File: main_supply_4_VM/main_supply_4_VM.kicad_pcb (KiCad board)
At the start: 2 copper layers, 108.6 x 131.8 mm, 197 parts, among them J1 Conn_01x02_Pin, J2 A3_EN, J3 A3, J4 A2, J5 A2_EN, J6 FIL_EN, J7 FIL CAT FOCUS, J8 Conn_01x02_Pin, Q1 CSD19537Q3, Q2 Si7450DP, Q3 CSD19537Q3, Q4 STN0214, Q5 2N7002, T2 750315839, T3 YA9033-ALD, U1 LM5155DSSR, U10 TLV314QDBVR, U11 TLV314QDBVR, U12 Opamp_sep_pwr, U2 TLV314QDBVR, U3 LM5155DSSR, U4 PC817, U5 LM5155DSSR, U6 TL431DBZ, U7 AP2204K-5.0, U8 AP2204K-5.0, U9 AMC1311

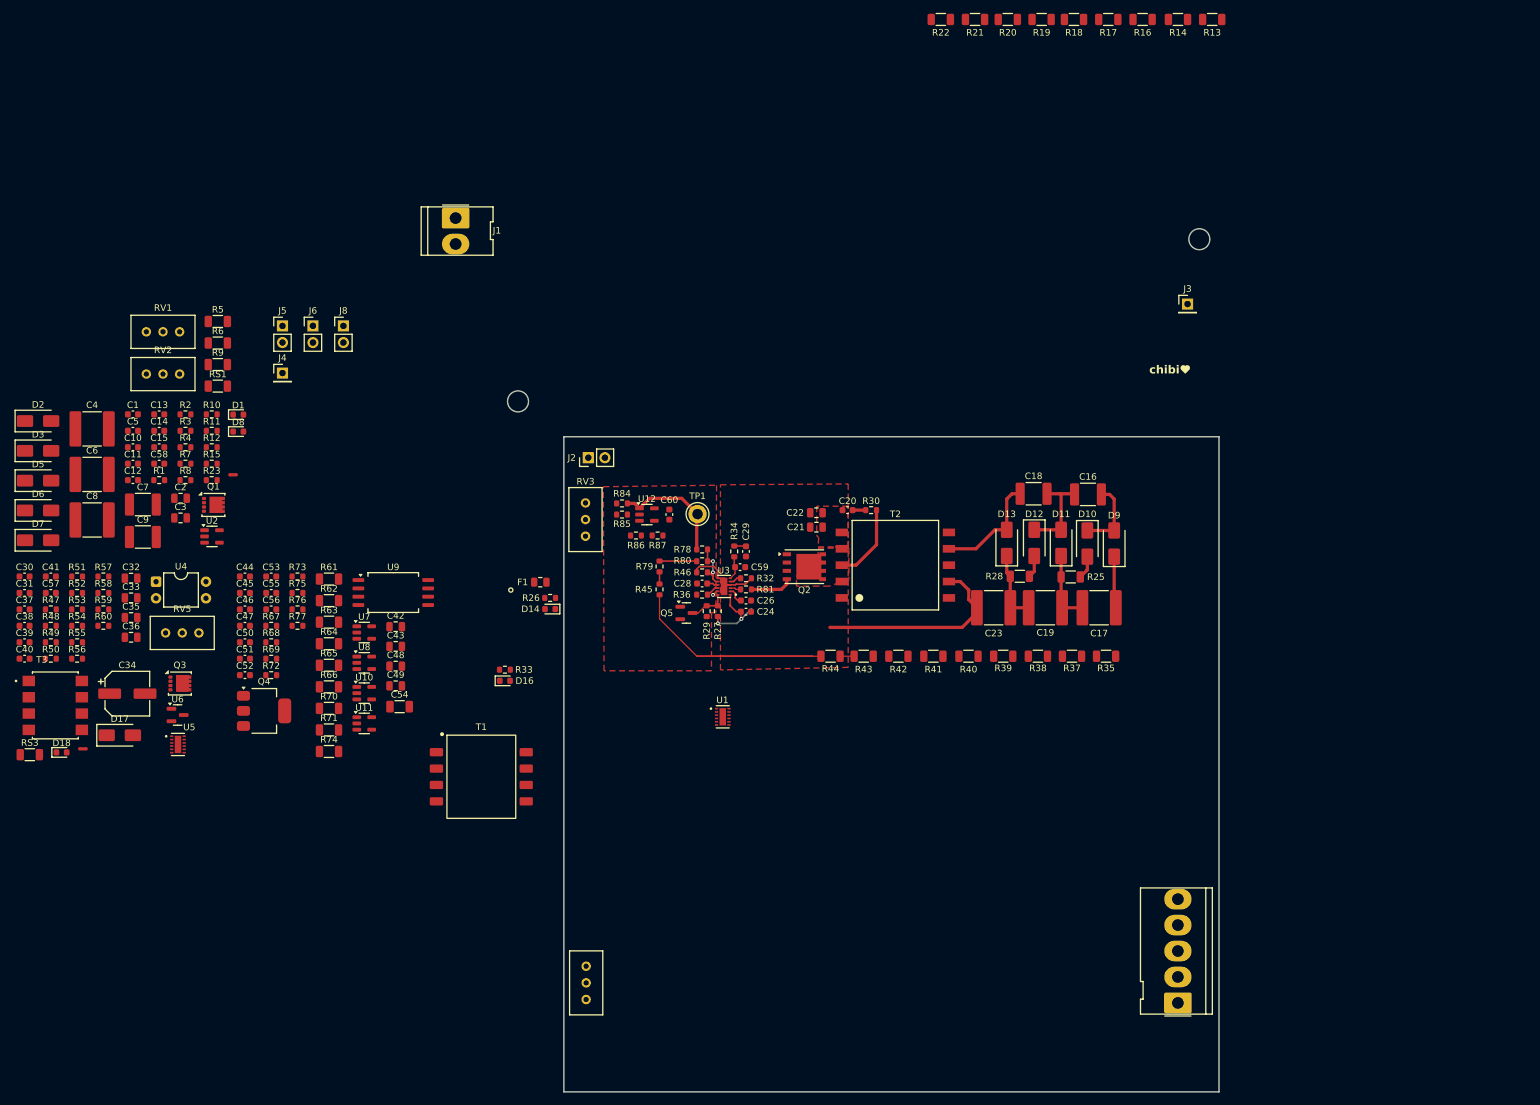
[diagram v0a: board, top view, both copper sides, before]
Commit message: finished routing and layout
need to update U6 stuff
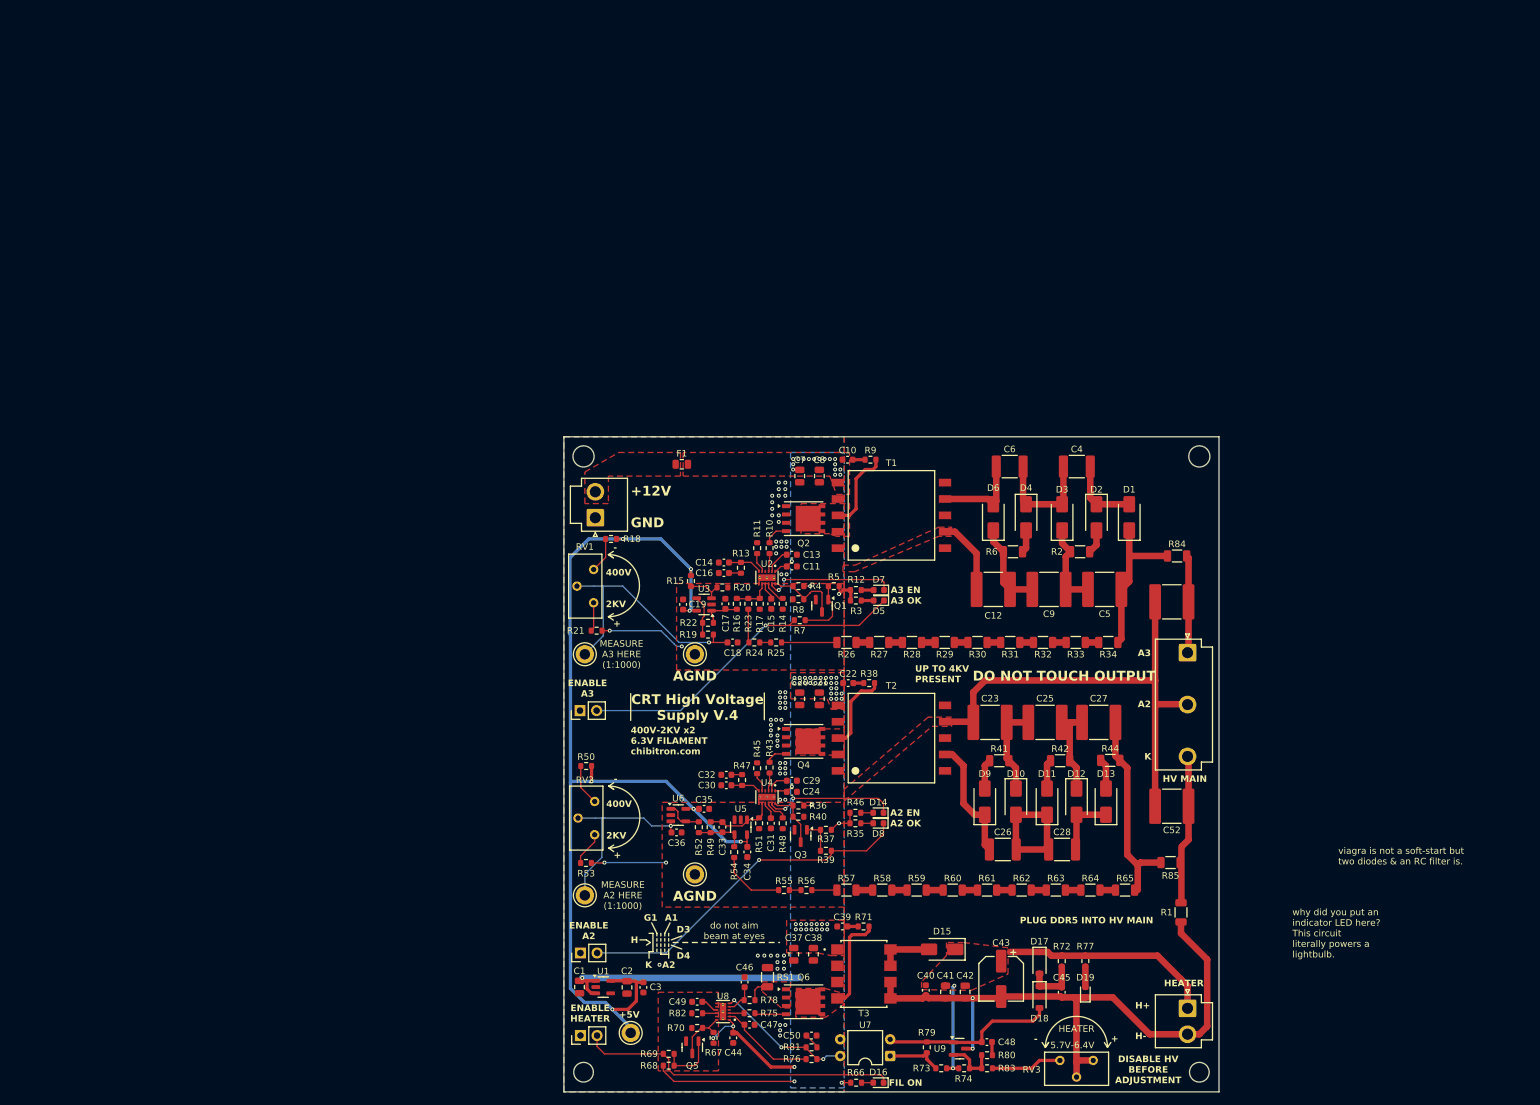
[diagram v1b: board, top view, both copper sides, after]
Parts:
- removed C53, C59: 100p, Capacitor_SMD:C_0603_1608Metric
- removed C54: 1n, Capacitor_SMD:C_1206_3216Metric
- removed C55, C56: 1n, Capacitor_SMD:C_0603_1608Metric
- removed C57: 1u, Capacitor_SMD:C_0603_1608Metric
- removed C58, C60: 100n, Capacitor_SMD:C_0603_1608Metric
- removed J7: FIL CAT FOCUS, Connector_Molex:Molex_KK-396_5273-05A_1x05_P3.96mm_Vertical
- removed J8: Conn_01x02_Pin, Connector_PinHeader_2.54mm:PinHeader_1x02_P2.54mm_Vertical
- removed R86, R87: R_US, Resistor_SMD:R_0603_1608Metric
- removed RS3: 0.002, Resistor_SMD:R_1206_3216Metric
- removed RV4, RV5: 4.7k, Potentiometer_THT:Potentiometer_Bourns_3296W_Vertical
- removed U10, U11: TLV314QDBVR, Package_TO_SOT_SMD:SOT-23-5
- removed U12: Opamp_sep_pwr, Package_TO_SOT_SMD:SOT-23-5
- added C25: 220n, Capacitor_SMD:C_2220_5750Metric, F.Cu at (173.4, 93.6)
- added C27: 220n, Capacitor_SMD:C_2220_5750Metric, F.Cu at (181.7, 93.6)
- added D15: D_Schottky, Diode_SMD:D_SMA, F.Cu at (157.7, 128.2)
- added D19: LED, LED_SMD:LED_0603_1608Metric, F.Cu at (179.6, 134.8)
- added D4: D, Diode_SMD:D_SMA, F.Cu at (170.6, 62.3)
- added Q6: Si7450DP, Package_SO:PowerPAK_SO-8_Single, F.Cu at (136.6, 136.2)
- added R24: 330k, Resistor_SMD:R_0603_1608Metric, F.Cu at (129.1, 81.4)
- added R31: 1Meg, Resistor_SMD:R_1206_3216Metric, F.Cu at (168.1, 81.4)
- added R82: 50k, Resistor_SMD:R_0603_1608Metric, F.Cu at (120.3, 138.0)
- added R83: 21k, Resistor_SMD:R_0603_1608Metric, F.Cu at (164.6, 146.4)
- added TP2: A2-ADJ, TestPoint:TestPoint_Keystone_5010-5014_Multipurpose, F.Cu at (103.2, 120.0)
- added TP3: AGND3, TestPoint:TestPoint_Keystone_5010-5014_Multipurpose, F.Cu at (120.0, 83.2)
- added TP4: AGND, TestPoint:TestPoint_Keystone_5010-5014_Multipurpose, F.Cu at (120.0, 116.8)
- added TP5: 5V, TestPoint:TestPoint_Keystone_5010-5014_Multipurpose, F.Cu at (110.2, 141.0)
- C1, C20: value 220p -> 10u; footprint Capacitor_SMD:C_0603_1608Metric -> Capacitor_SMD:C_0805_2012Metric
- C10: value 470p -> 220p
- C11: value 1u -> 100n
- C12: value 220p -> 220n; footprint Capacitor_SMD:C_0603_1608Metric -> Capacitor_SMD:C_2220_5750Metric
- C13: value 47n -> 1u
- C14: value 22n -> 100p
- C15: value 100p -> 47n
- C16: value 100n -> 470n; footprint Capacitor_SMD:C_1812_4532Metric -> Capacitor_SMD:C_0603_1608Metric
- C17: value 220n -> 100p; footprint Capacitor_SMD:C_2220_5750Metric -> Capacitor_SMD:C_0603_1608Metric
- C18: value 100n -> 100p; footprint Capacitor_SMD:C_1812_4532Metric -> Capacitor_SMD:C_0603_1608Metric
- C19: value 220n -> 100n; footprint Capacitor_SMD:C_2220_5750Metric -> Capacitor_SMD:C_0603_1608Metric
- C22: value 10u -> 220p; footprint Capacitor_SMD:C_0805_2012Metric -> Capacitor_SMD:C_0603_1608Metric
- C26: value 1u -> 100n; footprint Capacitor_SMD:C_0603_1608Metric -> Capacitor_SMD:C_1812_4532Metric
- C28: value 47n -> 100n; footprint Capacitor_SMD:C_0603_1608Metric -> Capacitor_SMD:C_1812_4532Metric
- C29: value 22n -> 1u
- C3, C35: value 10u -> 100n; footprint Capacitor_SMD:C_0805_2012Metric -> Capacitor_SMD:C_0603_1608Metric
- C30: value 220p -> 100p
- C31: value 100n -> 47n
- C32: value 10u -> 470n; footprint Capacitor_SMD:C_0805_2012Metric -> Capacitor_SMD:C_0603_1608Metric
- C33: value 10u -> 20p; footprint Capacitor_SMD:C_0805_2012Metric -> Capacitor_SMD:C_0603_1608Metric
- C34: value 100u -> 100n; footprint Capacitor_SMD:CP_Elec_6.3x7.7 -> Capacitor_SMD:C_0603_1608Metric
- C36: value 10u -> 100p; footprint Capacitor_SMD:C_0805_2012Metric -> Capacitor_SMD:C_0603_1608Metric
- C37: value 220n -> 10u; footprint Capacitor_SMD:C_0603_1608Metric -> Capacitor_SMD:C_0805_2012Metric
- C38: value 470p -> 10u; footprint Capacitor_SMD:C_0603_1608Metric -> Capacitor_SMD:C_0805_2012Metric
- C39: value 1u -> 220p
- C4, C6: value 220n -> 100n; footprint Capacitor_SMD:C_2220_5750Metric -> Capacitor_SMD:C_1812_4532Metric
- C40: value 220n -> 100n
- C41: value 47n -> 10u; footprint Capacitor_SMD:C_0603_1608Metric -> Capacitor_SMD:C_0805_2012Metric
- C43: value 10u -> 100u; footprint Capacitor_SMD:C_0805_2012Metric -> Capacitor_SMD:CP_Elec_6.3x7.7
- C45: value 100n -> C
- C46: value 100n -> 470p
- C47: value 100n -> 1u
- C48: value 10u -> 220n; footprint Capacitor_SMD:C_0805_2012Metric -> Capacitor_SMD:C_0603_1608Metric
- C49: value 10u -> 47n; footprint Capacitor_SMD:C_0805_2012Metric -> Capacitor_SMD:C_0603_1608Metric
- C5: value 100n -> 220n; footprint Capacitor_SMD:C_0603_1608Metric -> Capacitor_SMD:C_2220_5750Metric
- C50: value 100n -> 220n
- C51: value 100n -> 10n; footprint Capacitor_SMD:C_0603_1608Metric -> Capacitor_SMD:C_2220_5750Metric
- C52: value 1n -> 10n; footprint Capacitor_SMD:C_0603_1608Metric -> Capacitor_SMD:C_2220_5750Metric
- C7: value 100n -> 10u; footprint Capacitor_SMD:C_1812_4532Metric -> Capacitor_SMD:C_0805_2012Metric
- C8: value 220n -> 10u; footprint Capacitor_SMD:C_2220_5750Metric -> Capacitor_SMD:C_0805_2012Metric
- C9: value 100n -> 220n; footprint Capacitor_SMD:C_1812_4532Metric -> Capacitor_SMD:C_2220_5750Metric
- D1: value LED -> D; footprint LED_SMD:LED_0603_1608Metric -> Diode_SMD:D_SMA
- D17: value D -> D_Schottky; footprint Diode_SMD:D_SMA -> Diode_SMD:D_SOD-123
- D18: value LED -> D_Schottky; footprint LED_SMD:LED_0603_1608Metric -> Diode_SMD:D_SOD-123
- D5, D7: value D -> LED; footprint Diode_SMD:D_SMA -> LED_SMD:LED_0603_1608Metric
- J1: value Conn_01x02_Pin -> 12V IN; footprint Connector_Molex:Molex_KK-396_5273-02A_1x02_P3.96mm_Vertical -> Connector_JST:JST_VH_B2P-VH-B_1x02_P3.96mm_Vertical
- J3: value A3 -> A2_EN; footprint Connector_PinHeader_2.54mm:PinHeader_1x01_P2.54mm_Vertical -> Connector_PinHeader_2.54mm:PinHeader_1x02_P2.54mm_Vertical
- J4: value A2 -> FIL_EN; footprint Connector_PinHeader_2.54mm:PinHeader_1x01_P2.54mm_Vertical -> Connector_PinHeader_2.54mm:PinHeader_1x02_P2.54mm_Vertical
- J5: value A2_EN -> MAIN HV; footprint Connector_PinHeader_2.54mm:PinHeader_1x02_P2.54mm_Vertical -> JST_VH:JST_VH_B3P5-VH-B_1x05_P3.96mm_Vertical
- J6: value FIL_EN -> FILAMENT; footprint Connector_PinHeader_2.54mm:PinHeader_1x02_P2.54mm_Vertical -> Connector_JST:JST_VH_B2P-VH-B_1x02_P3.96mm_Vertical
- NT1, NT2, NT3: footprint NetTie:NetTie-2_SMD_Pad0.5mm -> NetTie:NetTie_0.2mm
- Q1, Q3: value CSD19537Q3 -> 2N7002; footprint Package_SON:VSON-8_3.3x3.3mm_P0.65mm_NexFET -> Package_TO_SOT_SMD:SOT-23
- Q4: value STN0214 -> Si7450DP; footprint Package_TO_SOT_SMD:SOT-223-3_TabPin2 -> Package_SO:PowerPAK_SO-8_Single
- R1: value 3.9k -> 1Meg; footprint Resistor_SMD:R_0603_1608Metric -> Resistor_SMD:R_1206_3216Metric
- R10: value 2k -> 0
- R11: value 22k -> 10k
- R12: value 100k -> 39k
- R13: value 1Meg -> 1k; footprint Resistor_SMD:R_1206_3216Metric -> Resistor_SMD:R_0603_1608Metric
- R14: value 1Meg -> 220k; footprint Resistor_SMD:R_1206_3216Metric -> Resistor_SMD:R_0603_1608Metric
- R15: value 470 -> R_US
- R16, R17, R19, R22, R39, R40, R70: value 1Meg -> 10k; footprint Resistor_SMD:R_1206_3216Metric -> Resistor_SMD:R_0603_1608Metric
- R18: value 1Meg -> 30k; footprint Resistor_SMD:R_1206_3216Metric -> Resistor_SMD:R_0603_1608Metric
- R2: value 50k -> 20; footprint Resistor_SMD:R_0603_1608Metric -> Resistor_SMD:R_1206_3216Metric
- R20: value 1Meg -> R_US; footprint Resistor_SMD:R_1206_3216Metric -> Resistor_SMD:R_0603_1608Metric
- R21: value 1Meg -> 2.4k; footprint Resistor_SMD:R_1206_3216Metric -> Resistor_SMD:R_0603_1608Metric
- R23: value 4.7k -> 330k
- R25: value 20 -> 330k; footprint Resistor_SMD:R_1206_3216Metric -> Resistor_SMD:R_0603_1608Metric
- R26: value 39k -> 1Meg; footprint Resistor_SMD:R_0603_1608Metric -> Resistor_SMD:R_1206_3216Metric
- R27, R60: value 50k -> 1Meg; footprint Resistor_SMD:R_0603_1608Metric -> Resistor_SMD:R_1206_3216Metric
- R28: value 20 -> 1Meg
- R29, R32: value 10k -> 1Meg; footprint Resistor_SMD:R_0603_1608Metric -> Resistor_SMD:R_1206_3216Metric
- R3: value 50k -> 39k
- R30: value 100 -> 1Meg; footprint Resistor_SMD:R_0603_1608Metric -> Resistor_SMD:R_1206_3216Metric
- R33, R58: value 2k -> 1Meg; footprint Resistor_SMD:R_0603_1608Metric -> Resistor_SMD:R_1206_3216Metric
- R34: value 22k -> 1Meg; footprint Resistor_SMD:R_0603_1608Metric -> Resistor_SMD:R_1206_3216Metric
- R35, R66: value 1Meg -> 39k; footprint Resistor_SMD:R_1206_3216Metric -> Resistor_SMD:R_0603_1608Metric
- R36: value 220k -> 50k
- R37: value 1Meg -> 100k; footprint Resistor_SMD:R_1206_3216Metric -> Resistor_SMD:R_0603_1608Metric
- R38: value 1Meg -> 100; footprint Resistor_SMD:R_1206_3216Metric -> Resistor_SMD:R_0603_1608Metric
- R4: value 100 -> 50k
- R41, R42, R44: value 1Meg -> 20
- R43: value 1Meg -> 0; footprint Resistor_SMD:R_1206_3216Metric -> Resistor_SMD:R_0603_1608Metric
- R45: value 330k -> 10k
- R46, R77: value 10k -> 22k
- R47: value 50k -> 1k
- R48: value 100 -> 220k
- R49: value 50k -> 25k
- R5: value 20 -> 100k; footprint Resistor_SMD:R_1206_3216Metric -> Resistor_SMD:R_0603_1608Metric
- R50: value 1k -> 30k
- R51: value 33k -> 4.7k
- R52: value 5k -> 10k
- R53: value 0 -> 2.4k
- R54, R55: value 1k -> 330k
- R56: value 20 -> 330k
- R57: value 1k -> 1Meg; footprint Resistor_SMD:R_0603_1608Metric -> Resistor_SMD:R_1206_3216Metric
- R59: value 20k -> 1Meg; footprint Resistor_SMD:R_0603_1608Metric -> Resistor_SMD:R_1206_3216Metric
- R67: value 6.8k -> 50k
- R7: value 0 -> 10k
- R71: value 100k -> 100; footprint Resistor_SMD:R_1206_3216Metric -> Resistor_SMD:R_0603_1608Metric
- R72: value 10k -> R_US
- R73: value 5k -> 1k
- R74: value 1Meg -> 33k; footprint Resistor_SMD:R_1206_3216Metric -> Resistor_SMD:R_0603_1608Metric
- R75: value 10k -> 0
- R76: value 10k -> 5k
- R78: value 10k -> 20
- R79, R80: value 330k -> 1k
- R8: value 20 -> 10k
- R81: value 0 -> 1k
- R84, R85: value 10k -> 1.5k; footprint Resistor_SMD:R_0603_1608Metric -> Resistor_SMD:R_1206_3216Metric
- R9: value 20 -> 100; footprint Resistor_SMD:R_1206_3216Metric -> Resistor_SMD:R_0603_1608Metric
- RS1: value 0.002 -> 0.02
- RV1: value 1Meg -> 10k; footprint Potentiometer_THT:Potentiometer_Bourns_3296W_Vertical -> Potentiometer_THT:Potentiometer_Bourns_3296Y_Vertical
- RV2: value 4.7k -> 10k; footprint Potentiometer_THT:Potentiometer_Bourns_3296W_Vertical -> Potentiometer_THT:Potentiometer_Bourns_3296Y_Vertical
- RV3: value 10k -> 4.7k; footprint Potentiometer_THT:Potentiometer_Bourns_3296W_Vertical -> Potentiometer_THT:Potentiometer_Bourns_3296Y_Vertical
- T1: value ~ -> 750315839; footprint coilcraft:NA5920-AL -> 750315839:WE-FLYLT_EP13_5465
- TP1: value TestPoint -> A3-ADJ
- U1: value LM5155DSSR -> AP2204K-5.0; footprint LM5155:IC_LM5155DSSR -> Package_TO_SOT_SMD:SOT-23-5
- U2: value TLV314QDBVR -> LM5155DSSR; footprint Package_TO_SOT_SMD:SOT-23-5 -> LM5155DSSR:IC_LM5155DSSR
- U3, U5: value LM5155DSSR -> TLV314QDBVR; footprint LM5155:IC_LM5155DSSR -> Package_TO_SOT_SMD:SOT-23-5
- U4: value PC817 -> LM5155DSSR; footprint Package_DIP:DIP-4_W7.62mm -> LM5155DSSR:IC_LM5155DSSR
- U6: value TL431DBZ -> TLV314QDBVR; footprint Package_TO_SOT_SMD:SOT-23 -> Package_TO_SOT_SMD:SOT-23-5
- U7: value AP2204K-5.0 -> PC817; footprint Package_TO_SOT_SMD:SOT-23-5 -> Package_DIP:DIP-4_W7.62mm
- U8: value AP2204K-5.0 -> LM5155DSSR; footprint Package_TO_SOT_SMD:SOT-23-5 -> LM5155DSSR:IC_LM5155DSSR
- U9: value AMC1311 -> TL431DBZ; footprint Package_SO:SOIC-8_7.5x5.85mm_P1.27mm -> Package_TO_SOT_SMD:SOT-23
- moved R1 169.4 mm to (194.2, 122.6), turned to -90 degrees
- moved J6 169.3 mm to (195.2, 137.2), turned to -90 degrees
- moved D2 162.2 mm to (181.3, 62.3), turned to -90 degrees
- moved D3 156.6 mm to (176.1, 62.3), turned to 90 degrees
- moved D18 153.9 mm to (172.6, 135.5), turned to -90 degrees
- moved C41 150.6 mm to (158.2, 134.7), turned to -90 degrees
- moved C4 150.4 mm to (178.3, 54.5)
- moved C5 150.3 mm to (182.6, 73.3)
- moved J5 146.9 mm to (195.2, 83.0), turned to -90 degrees
- moved C40 146.6 mm to (155.2, 134.5), turned to -90 degrees
- moved D6 145.8 mm to (165.6, 62.3), turned to 90 degrees
- moved D17 144.6 mm to (172.6, 130.3), turned to -90 degrees
- moved C52 142.9 mm to (192.8, 106.4), turned to 180 degrees
- moved C51 141.8 mm to (192.8, 75.2), turned to 180 degrees
- moved C6 140.1 mm to (168.1, 54.5)
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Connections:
- C1 pad 1: /A2 Supply/+12V_IN -> +12V
- C1 pad 2: Net-(C1-Pad2) -> GND
- C10 pad 1: /A2 Supply/CS_FILT -> +12V
- C10 pad 2: GND -> Net-(C10-Pad2)
- C11 pad 1: /A2 Supply/VCC -> +12V
- C12 pad 1: Net-(U1-COMP) -> GND
- C12 pad 2: Net-(C12-Pad2) -> Net-(D6-K)
- C13 pad 1: Net-(U1-SS) -> /A3 Supply/VCC
- C13 pad 2: AGND -> GND
- C14 pad 1: Net-(C14-Pad1) -> Net-(U2-COMP)
- C14 pad 2: Net-(C12-Pad2) -> GND
- C15 pad 1: /A2 Supply/FB_HV -> Net-(U2-SS)
- C15 pad 2: /A2 Supply/FB_HV_LADDER -> AGND3
- C16 pad 1: Net-(D11-A) -> Net-(C16-Pad1)
- C16 pad 2: Net-(D10-K) -> GND
- C17 pad 1: Net-(D11-K) -> /A3 Supply/OUTPUT_ADJ
- C17 pad 2: /A3 Supply/+PDA -> AGND3
- C18 pad 1: Net-(D13-A) -> Net-(C18-Pad1)
- C18 pad 2: Net-(D11-A) -> AGND3
- C19 pad 1: Net-(D13-K) -> +5V
- C19 pad 2: Net-(D11-K) -> AGND3
- C2 pad 1: /A2 Supply/+12V_IN -> +5V
- C20 pad 2: Net-(C20-Pad2) -> GND
- C22 pad 2: GND -> Net-(C22-Pad2)
- C23 pad 2: Net-(D13-K) -> Net-(D10-K)
- C26 pad 1: /A3 Supply/VCC -> Net-(D9-K)
- C26 pad 2: GND -> Net-(D10-A)
- C28 pad 1: Net-(U3-SS) -> Net-(D10-A)
- C28 pad 2: AGND3 -> Net-(D12-A)
- C29 pad 1: Net-(C29-Pad1) -> /A2 Supply/VCC
- C3 pad 1: /A2 Supply/+12V_IN -> +5V
- C30 pad 1: /FIL_+12V -> Net-(U4-COMP)
- C30 pad 2: Net-(C30-Pad2) -> GND
- C31 pad 1: /Filament Supply/FILAMENT -> Net-(U4-SS)
- C31 pad 2: /A2 Supply/CATHODE -> AGND
- C32 pad 1: /Filament Supply/FILAMENT -> Net-(C32-Pad1)
- C32 pad 2: /A2 Supply/CATHODE -> GND
- C33 pad 1: /Filament Supply/FILAMENT -> /A2 Supply/FB_HV
- C33 pad 2: /A2 Supply/CATHODE -> /A2 Supply/FB_HV_LADDER
- C34 pad 1: /Filament Supply/FILAMENT -> +5V
- C34 pad 2: /A2 Supply/CATHODE -> AGND
- C35 pad 1: /FIL_+12V -> +5V
- C35 pad 2: GND -> AGND
- C36 pad 1: /FIL_+12V -> Net-(U6-+)
- C36 pad 2: GND -> AGND
- C37 pad 1: Net-(U6-K) -> +12V
- C37 pad 2: Net-(C37-Pad2) -> GND
- C38 pad 1: /Filament Supply/CS_FIL -> +12V
- C39 pad 1: /Filament Supply/VCC_FIL -> +12V
- C39 pad 2: GND -> Net-(C39-Pad2)
- C4 pad 1: GND -> Net-(D3-A)
- C4 pad 2: Net-(D3-K) -> Net-(D1-A)
- C40 pad 1: Net-(C40-Pad1) -> /Filament Supply/FILAMENT
- C40 pad 2: GND -> /Filament Supply/CATHODE
- C41 pad 1: Net-(U5-SS) -> /Filament Supply/FILAMENT
- C41 pad 2: AGND2 -> /Filament Supply/CATHODE
- C42 pad 2: /A2 Supply/CATHODE -> /Filament Supply/CATHODE
- C43 pad 1: Net-(U10-V+) -> /Filament Supply/FILAMENT
- C43 pad 2: /A2 Supply/CATHODE -> /Filament Supply/CATHODE
- C44 pad 1: Net-(U10-V+) -> +12V
- C44 pad 2: /A2 Supply/CATHODE -> GND
- C45 pad 1: Net-(U10-V+) -> Net-(D17-A)
- C45 pad 2: /A2 Supply/CATHODE -> /Filament Supply/CATHODE
- C46 pad 1: +5V -> /Filament Supply/CS_FIL
- C47 pad 1: Net-(U10-V+) -> /Filament Supply/VCC_FIL
- C47 pad 2: /A2 Supply/CATHODE -> GND
- C48 pad 1: /FIL_+12V -> Net-(D18-A)
- C48 pad 2: GND -> Net-(C48-Pad2)
- C49 pad 1: +5V -> Net-(U8-SS)
- C49 pad 2: GND -> AGND2
- C5 pad 1: /A2 Supply/+12V_IN -> Net-(D3-K)
- C5 pad 2: GND -> /A3 Supply/PDA_FB
- C50 pad 1: +5V -> Net-(C50-Pad1)
- C51 pad 1: Net-(U10-V+) -> /A3 Supply/+PDA
- C51 pad 2: /A2 Supply/CATHODE -> GND
- C52 pad 1: /A2 Supply/CATHODE -> /A2 Supply/-2KV
- C52 pad 2: Net-(U10-+) -> GND
- C6 pad 1: Net-(D3-K) -> Net-(D6-A)
- C6 pad 2: Net-(D6-K) -> Net-(D3-A)
- C7 pad 1: Net-(D2-K) -> +12V
- C7 pad 2: Net-(D3-A) -> GND
- C8 pad 1: Net-(D6-K) -> +12V
- C8 pad 2: /-2KV -> GND
- C9 pad 1: Net-(D3-A) -> Net-(D6-K)
- C9 pad 2: Net-(D6-A) -> Net-(D3-K)
- D1 pad 1: GND -> /A3 Supply/PDA_FB
- D11 pad 1: Net-(D11-K) -> Net-(D10-A)
- D12 pad 1: Net-(D11-A) -> Net-(D12-K)
- D13 pad 1: Net-(D13-K) -> Net-(D12-A)
- D14 pad 1: /A3 Supply/EN -> /A2 Supply/PGOOD_HV
- D16 pad 1: /A3 Supply/PGOOD_HV -> /Filament Supply/EN
- D18 pad 1: /Filament Supply/PGOOD_FIL -> Net-(D17-A)
- D2 pad 1: Net-(D2-K) -> Net-(D1-A)
- D5 pad 1: Net-(D3-A) -> /A3 Supply/EN
- D7 pad 1: Net-(D6-A) -> /A3 Supply/PGOOD_HV
- D8 pad 1: /A2 Supply/PGOOD_HV -> /A2 Supply/EN
- D9 pad 1: /A3 Supply/+PDA -> Net-(D9-K)
- D9 pad 2: Net-(D10-K) -> Net-(D9-A)
- F1 pad 1: Net-(J1-Pin_1) -> /12V_IN
- J1 pad 1: Net-(J1-Pin_1) -> GND
- J1 pad 2: GND -> /12V_IN
- J3 pad 1: /A3 Supply/+PDA -> GND
- J5 pad 1: +12V -> /A3 Supply/+PDA
- J6 pad 1: +12V -> /Filament Supply/FILAMENT
- J6 pad 2: /FIL_+12V -> /Filament Supply/CATHODE
- NT1 pad 1: AGND -> AGND3
- NT2 pad 1: AGND3 -> AGND
- Q1 pad 1: /A2 Supply/CS -> Net-(Q1-G)
- Q1 pad 2: /A2 Supply/CS -> AGND3
- Q1 pad 3: /A2 Supply/CS -> /A3 Supply/UVLO
- Q2 pad 5: Net-(Q2-D) -> /A3 Supply/GATE_DRAIN
- Q3 pad 1: /Filament Supply/MOS_SOURCE_FIL -> Net-(Q3-G)
- Q3 pad 2: /Filament Supply/MOS_SOURCE_FIL -> AGND
- Q3 pad 3: /Filament Supply/MOS_SOURCE_FIL -> /A2 Supply/UVLO
- Q4 pad 1: Net-(Q4-C) -> GND
- Q4 pad 2: Net-(Q4-B) -> GND
- Q4 pad 3: /A2 Supply/CATHODE -> GND
- Q5 pad 2: AGND3 -> AGND2
- Q5 pad 3: /A3 Supply/UVLO -> /Filament Supply/UVLO
- R1 pad 1: /A2 Supply/+12V_IN -> /A2 Supply/-2KV
- R1 pad 2: Net-(D1-A) -> /Filament Supply/CATHODE
- R10 pad 1: /A2 Supply/VCC -> Net-(U2-GATE)
- R10 pad 2: Net-(D8-A) -> Net-(Q2-G)
- R11 pad 1: Net-(U1-COMP) -> Net-(U2-CS)
- R11 pad 2: Net-(C14-Pad1) -> GND
- R12 pad 1: Net-(U1-RT) -> +12V
- R12 pad 2: AGND -> Net-(D7-A)
- R13 pad 1: /A2 Supply/BRIGHTNESS -> Net-(U2-COMP)
- R13 pad 2: Net-(R13-Pad2) -> Net-(C16-Pad1)
- R14 pad 1: Net-(R13-Pad2) -> Net-(U2-RT)
- R14 pad 2: Net-(R14-Pad2) -> AGND3
- R15 pad 1: /A2 Supply/FB_HV -> +5V
- R15 pad 2: Net-(R15-Pad2) -> Net-(U3-+)
- R16 pad 1: Net-(R14-Pad2) -> /A3 Supply/OUTPUT_ADJ
- R16 pad 2: Net-(R16-Pad2) -> /A3 Supply/FB_PDA
- R17 pad 1: Net-(R16-Pad2) -> AGND3
- R17 pad 2: Net-(R17-Pad2) -> /A3 Supply/FB_PDA
- R18 pad 1: Net-(R18-Pad1) -> +5V
- R18 pad 2: Net-(R17-Pad2) -> Net-(R18-Pad2)
- R19 pad 1: Net-(R19-Pad1) -> Net-(U3--)
- R19 pad 2: Net-(R18-Pad1) -> Net-(C18-Pad1)
- R2 pad 1: /A2 Supply/+12V_IN -> Net-(D3-K)
- R2 pad 2: /A2 Supply/UVLO -> Net-(D2-A)
- R20 pad 1: Net-(R20-Pad1) -> Net-(U3-+)
- R20 pad 2: Net-(R19-Pad1) -> AGND3
- R21 pad 2: Net-(R20-Pad1) -> AGND3
- R22 pad 1: /A2 Supply/FB_HV_LADDER -> /A3 Supply/OUTPUT_ADJ
- R22 pad 2: Net-(R21-Pad1) -> Net-(U3--)
- R23 pad 1: /A2 Supply/FB_HV -> Net-(R23-Pad1)
- R23 pad 2: GND -> /A3 Supply/FB_PDA
- R25 pad 1: Net-(D11-K) -> Net-(R25-Pad1)
- R25 pad 2: Net-(D10-A) -> Net-(R24-Pad1)
- R26 pad 1: +12V -> Net-(R26-Pad1)
- R26 pad 2: Net-(D14-A) -> Net-(R25-Pad1)
- R27 pad 1: +12V -> Net-(R27-Pad1)
- R27 pad 2: /A3 Supply/UVLO -> Net-(R26-Pad1)
- R28 pad 1: Net-(D13-K) -> Net-(R28-Pad1)
- R28 pad 2: Net-(D12-A) -> Net-(R27-Pad1)
- R29 pad 1: /A3 Supply/UVLO -> Net-(R29-Pad1)
- R29 pad 2: AGND3 -> Net-(R28-Pad1)
- R3 pad 1: /A2 Supply/UVLO -> +12V
- R3 pad 2: GND -> Net-(D5-A)
- R30 pad 1: Net-(C20-Pad2) -> Net-(R30-Pad1)
- R30 pad 2: Net-(Q2-D) -> Net-(R29-Pad1)
- R32 pad 1: Net-(U3-CS) -> Net-(R32-Pad1)
- R32 pad 2: GND -> Net-(R31-Pad1)
- R33 pad 1: /A3 Supply/VCC -> Net-(R33-Pad1)
- R33 pad 2: Net-(D16-A) -> Net-(R32-Pad1)
- R34 pad 1: Net-(U3-COMP) -> /A3 Supply/PDA_FB
- R34 pad 2: Net-(C29-Pad1) -> Net-(R33-Pad1)
- R35 pad 1: /A3 Supply/+PDA -> +12V
- R35 pad 2: Net-(R35-Pad2) -> Net-(D8-A)
- R36 pad 1: Net-(U3-RT) -> +12V
- R36 pad 2: AGND3 -> /A2 Supply/UVLO
- R37 pad 1: Net-(R35-Pad2) -> Net-(Q3-G)
- R37 pad 2: Net-(R37-Pad2) -> +12V
- R38 pad 1: Net-(R37-Pad2) -> Net-(C22-Pad2)
- R38 pad 2: Net-(R38-Pad2) -> /A2 Supply/GATE_DRAIN
- R39 pad 1: Net-(R38-Pad2) -> /A2 Supply/EN
- R39 pad 2: Net-(R39-Pad2) -> Net-(Q3-G)
- R4 pad 1: Net-(C1-Pad2) -> +12V
- R4 pad 2: /A2 Supply/MOS_DRAIN -> /A3 Supply/UVLO
- R40 pad 1: Net-(R39-Pad2) -> /A2 Supply/UVLO
- R40 pad 2: Net-(R40-Pad2) -> AGND
- R41 pad 1: Net-(R41-Pad1) -> Net-(D9-A)
- R41 pad 2: Net-(R40-Pad2) -> Net-(D10-K)
- R42 pad 1: Net-(R42-Pad1) -> Net-(D11-A)
- R42 pad 2: Net-(R41-Pad1) -> Net-(D12-K)
- R43 pad 1: /A3 Supply/HV_FB2 -> Net-(U4-GATE)
- R43 pad 2: Net-(R42-Pad1) -> Net-(Q4-G)
- R44 pad 1: /A3 Supply/HV_FB1 -> Net-(D13-A)
- R44 pad 2: /A3 Supply/HV_FB2 -> /A2 Supply/A2_FB
- R45 pad 1: Net-(R45-Pad1) -> Net-(U4-CS)
- R45 pad 2: /A3 Supply/HV_FB1 -> GND
- R46 pad 1: AGND3 -> +12V
- R46 pad 2: /A3 Supply/FB_PDA -> Net-(D14-A)
- R47 pad 1: /FIL_+12V -> Net-(U4-COMP)
- R47 pad 2: /Filament Supply/UVLO -> Net-(C32-Pad1)
- R48 pad 1: Net-(C30-Pad2) -> Net-(U4-RT)
- R48 pad 2: /Filament Supply/MOS_DRAIN_FIL -> AGND
- R49 pad 1: /Filament Supply/UVLO -> /A2 Supply/FB_HV
- R49 pad 2: GND -> /A2 Supply/FB_HV_LADDER
- R5 pad 1: Net-(D2-A) -> Net-(Q1-G)
- R5 pad 2: Net-(D3-K) -> +12V
- R50 pad 1: /Filament Supply/FILAMENT -> +5V
- R51 pad 1: /Filament Supply/FILAMENT -> /A2 Supply/FB_HV
- R51 pad 2: Net-(U6-REF) -> AGND
- R52 pad 1: /Filament Supply/VCC_FIL -> /A2 Supply/FB_HV_LADDER
- R52 pad 2: Net-(R52-Pad2) -> Net-(U6--)
- R53 pad 1: /Filament Supply/GATE_FIL -> Net-(R53-Pad1)
- R53 pad 2: /Filament Supply/MOS_GATE_FIL -> AGND
- R54 pad 1: Net-(R50-Pad2) -> Net-(R54-Pad1)
- R54 pad 2: Net-(U6-K) -> /A2 Supply/FB_HV_LADDER
- R55 pad 1: Net-(C37-Pad2) -> Net-(R55-Pad1)
- R55 pad 2: Net-(U6-REF) -> Net-(R54-Pad1)
- R56 pad 1: /Filament Supply/CS_FIL -> Net-(R56-Pad1)
- R56 pad 2: /Filament Supply/MOS_SOURCE_FIL -> Net-(R55-Pad1)
- R57 pad 1: /Filament Supply/COMP_FB_FIL -> Net-(R57-Pad1)
- R57 pad 2: Net-(C40-Pad1) -> Net-(R56-Pad1)
- R58 pad 1: /Filament Supply/VCC_FIL -> Net-(R58-Pad1)
- R58 pad 2: Net-(D18-A) -> Net-(R57-Pad1)
- R59 pad 1: Net-(U6-REF) -> Net-(R59-Pad1)
- R59 pad 2: Net-(R59-Pad2) -> Net-(R58-Pad1)
- R6 pad 1: Net-(D5-A) -> Net-(D6-K)
- R6 pad 2: Net-(D6-K) -> Net-(D4-A)
- R60 pad 1: Net-(U5-RT) -> Net-(R60-Pad1)
- R60 pad 2: AGND2 -> Net-(R59-Pad1)
- R61 pad 1: GND -> Net-(R61-Pad1)
- R61 pad 2: Net-(R61-Pad2) -> Net-(R60-Pad1)
- R62 pad 1: Net-(R61-Pad2) -> Net-(R62-Pad1)
- R62 pad 2: Net-(R62-Pad2) -> Net-(R61-Pad1)
- R63 pad 1: Net-(R62-Pad2) -> Net-(R63-Pad1)
- R63 pad 2: Net-(Q4-C) -> Net-(R62-Pad1)
- R64 pad 1: Net-(Q4-C) -> Net-(R64-Pad1)
- R64 pad 2: Net-(R64-Pad2) -> Net-(R63-Pad1)
- R65 pad 1: Net-(R64-Pad2) -> /A2 Supply/A2_FB
- R65 pad 2: Net-(R65-Pad2) -> Net-(R64-Pad1)
- R66 pad 1: Net-(R65-Pad2) -> +12V
- R66 pad 2: Net-(R66-Pad2) -> Net-(D16-A)
- R67 pad 1: +5V -> +12V
- R67 pad 2: Net-(R67-Pad2) -> /Filament Supply/UVLO
- R68 pad 1: Net-(U11--) -> Net-(Q5-G)
- R68 pad 2: Net-(C53-Pad1) -> +12V
- R69 pad 1: /A2 Supply/CATHODE -> /Filament Supply/EN
- R69 pad 2: Net-(U10-+) -> Net-(Q5-G)
- R7 pad 1: Net-(U1-GATE) -> /A3 Supply/EN
- R70 pad 1: Net-(R66-Pad2) -> /Filament Supply/UVLO
- R70 pad 2: Net-(R70-Pad2) -> AGND2
- R71 pad 1: Net-(Q4-C) -> Net-(C39-Pad2)
- R71 pad 2: /Focus Amp/FOCUS -> /Filament Supply/MOS_DRAIN_FIL
- R72 pad 1: Net-(U9-+) -> /Filament Supply/FILAMENT
- R72 pad 2: Net-(U10-+) -> Net-(D17-A)
- R73 pad 1: Net-(C55-Pad2) -> /Filament Supply/FILAMENT
- R73 pad 2: Net-(U11--) -> Net-(R73-Pad2)
- R74 pad 1: Net-(R70-Pad2) -> /Filament Supply/FILAMENT
- R74 pad 2: Net-(U11-+) -> Net-(U9-REF)
- R75 pad 1: Net-(U9--) -> Net-(U8-GATE)
- R75 pad 2: Net-(U10--) -> Net-(Q6-G)
- R76 pad 1: Net-(U10--) -> /Filament Supply/VCC_FIL
- R76 pad 2: Net-(C55-Pad2) -> /Filament Supply/COMP_FB_FIL
- R77 pad 1: Net-(U11-+) -> /Filament Supply/FILAMENT
- R77 pad 2: /A2 Supply/CATHODE -> Net-(D19-A)
- R78 pad 1: /A3 Supply/OUTPUT_ADJ -> /Filament Supply/CS_FIL
- R78 pad 2: /A3 Supply/FB_PDA -> /Filament Supply/MOS_SOURCE_FIL
- R79 pad 1: Net-(R79-Pad1) -> Net-(R73-Pad2)
- R79 pad 2: Net-(R45-Pad1) -> Net-(D18-A)
- R8 pad 1: /A2 Supply/CS_FILT -> /A3 Supply/UVLO
- R8 pad 2: /A2 Supply/CS -> AGND3
- R80 pad 1: /A3 Supply/FB_PDA -> Net-(C48-Pad2)
- R80 pad 2: Net-(R79-Pad1) -> Net-(U9-REF)
- R81 pad 1: Net-(U3-GATE) -> /Filament Supply/COMP_FB_FIL
- R81 pad 2: Net-(Q2-G) -> Net-(C50-Pad1)
- R84 pad 1: /A3 Supply/OUTPUT_ADJ -> /A3 Supply/PDA_FB
- R84 pad 2: Net-(U12A--) -> /A3 Supply/+PDA
- R85 pad 1: Net-(U12A--) -> /A2 Supply/A2_FB
- R85 pad 2: Net-(C27-Pad1) -> /A2 Supply/-2KV
- R9 pad 1: Net-(D7-A) -> Net-(C10-Pad2)
- R9 pad 2: /-2KV -> /A3 Supply/GATE_DRAIN
- RS1 pad 1: /A2 Supply/CS -> /Filament Supply/MOS_SOURCE_FIL
- RV1 pad 1: /-2KV -> Net-(R21-Pad1)
- RV1 pad 2: /A2 Supply/CATHODE -> Net-(C18-Pad1)
- RV1 pad 3: /A2 Supply/BRIGHTNESS -> Net-(R18-Pad2)
- RV2 pad 1: Net-(R15-Pad2) -> Net-(R53-Pad1)
- RV2 pad 2: Net-(R15-Pad2) -> Net-(U6-+)
- RV2 pad 3: /A2 Supply/FB_HV_LADDER -> Net-(R50-Pad2)
- RV3 pad 1: Net-(R82-Pad2) -> /Filament Supply/CATHODE
- RV3 pad 2: Net-(C27-Pad1) -> /Filament Supply/CATHODE
- T1 pad 1: /A2 Supply/+12V_IN -> unconnected-(T1-Pad1)
- T1 pad 2: /A2 Supply/+12V_IN -> unconnected-(T1-Pad2)
- T1 pad 3: /A2 Supply/MOS_DRAIN -> /A3 Supply/GATE_DRAIN
- T1 pad 4: /A2 Supply/MOS_DRAIN -> unconnected-(T1-Pad4)
- T1 pad 5: GND -> +12V
- T1 pad 6: (no net) -> unconnected-(T1-Pad6)
- T1 pad 7: (no net) -> Net-(D6-A)
- T1 pad 8: Net-(D2-K) -> unconnected-(T1-Pad8)
- T2 pad 1: (no net) -> unconnected-(T2-Pad1)
- T2 pad 10: (no net) -> unconnected-(T2-Pad10)
- T2 pad 2: (no net) -> unconnected-(T2-Pad2)
- T2 pad 3: Net-(Q2-D) -> /A2 Supply/GATE_DRAIN
- T2 pad 4: (no net) -> unconnected-(T2-Pad4)
- T2 pad 6: (no net) -> unconnected-(T2-Pad6)
- T2 pad 7: Net-(D13-A) -> GND
- T2 pad 9: GND -> Net-(D9-K)
- T3 pad 1: /FIL_+12V -> +12V
- T3 pad 2: (no net) -> unconnected-(T3-Pad2)
- T3 pad 3: (no net) -> unconnected-(T3-Pad3)
- T3 pad 5: /A2 Supply/CATHODE -> /Filament Supply/CATHODE
- T3 pad 6: /A2 Supply/CATHODE -> /Filament Supply/CATHODE
- T3 pad 7: Net-(D17-A) -> Net-(D15-A)
- T3 pad 8: Net-(D17-A) -> Net-(D15-A)
- TP1 pad 1: /A3 Supply/OUTPUT_ADJ -> Net-(C18-Pad1)
- U1 pad 1: /A2 Supply/+12V_IN -> +12V
- U1 pad 2: /A2 Supply/VCC -> GND
- U1 pad 3: Net-(U1-GATE) -> +12V
- U1 pad 4: GND -> unconnected-(U1-NC-Pad4)
- U1 pad 5: /A2 Supply/CS_FILT -> +5V
- U2 pad 1: /A2 Supply/FB_HV -> +12V
- U2 pad 2: GND -> /A3 Supply/VCC
- U2 pad 3: GND -> Net-(U2-GATE)
- U2 pad 4: /A2 Supply/FB_HV_LADDER -> GND
- U2 pad 5: +5V -> Net-(U2-CS)
- U3 pad 1: +12V -> /A3 Supply/OUTPUT_ADJ
- U3 pad 2: /A3 Supply/VCC -> AGND3
- U3 pad 3: Net-(U3-GATE) -> Net-(U3-+)
- U3 pad 4: GND -> Net-(U3--)
- U3 pad 5: Net-(U3-CS) -> +5V
- U4 pad 1: Net-(R50-Pad2) -> +12V
- U4 pad 2: Net-(U6-K) -> /A2 Supply/VCC
- U4 pad 3: /Filament Supply/COMP_FB_FIL -> Net-(U4-GATE)
- U4 pad 4: Net-(R52-Pad2) -> GND
- U5 pad 1: /FIL_+12V -> /A2 Supply/FB_HV
- U5 pad 2: /Filament Supply/VCC_FIL -> AGND
- U5 pad 3: /Filament Supply/GATE_FIL -> AGND
- U5 pad 4: GND -> /A2 Supply/FB_HV_LADDER
- U5 pad 5: /Filament Supply/CS_FIL -> +5V
- U6 pad 1: Net-(U6-K) -> Net-(U6--)
- U6 pad 2: Net-(U6-REF) -> AGND
- U6 pad 3: /A2 Supply/CATHODE -> Net-(U6-+)
- U7 pad 1: /Filament Supply/FILAMENT -> Net-(R73-Pad2)
- U7 pad 2: /A2 Supply/CATHODE -> Net-(D18-A)
- U7 pad 3: /Filament Supply/FILAMENT -> GND
- U7 pad 4: unconnected-(U7-NC-Pad4) -> /Filament Supply/COMP_FB_FIL
- U8 pad 1: /FIL_+12V -> +12V
- U8 pad 2: GND -> /Filament Supply/VCC_FIL
- U8 pad 3: /FIL_+12V -> Net-(U8-GATE)
- U8 pad 4: unconnected-(U8-NC-Pad4) -> GND
- U8 pad 5: +5V -> /Filament Supply/CS_FIL
- U9 pad 1: +5V -> Net-(D18-A)
- U9 pad 2: /Focus Amp/FOCUS_ADJ -> Net-(U9-REF)
- U9 pad 3: GND -> /Filament Supply/CATHODE
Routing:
- net +5V: track 0.00 -> 160.0 mm, vias 0 -> 7
- net /Filament Supply/CATHODE: track 0.00 -> 96.1 mm, vias 0 -> 2
- net +12V: track 12.2 -> 97.5 mm, vias 2 -> 68
- net /A2 Supply/EN: track 0.00 -> 53.2 mm, vias 0 -> 1
- net /A3 Supply/EN: track 0.00 -> 52.1 mm, vias 0 -> 1
- net GND: track 36.0 -> 85.5 mm, vias 0 -> 60
- net /Filament Supply/EN: track 0.00 -> 49.1 mm
- net /A3 Supply/HV_FB1: track 48.3 -> 0.00 mm
- net /Filament Supply/FILAMENT: track 0.00 -> 47.3 mm, vias 0 -> 2
- net Net-(C18-Pad1): track 0.00 -> 39.3 mm, vias 0 -> 1
- net /A2 Supply/A2_FB: track 0.00 -> 30.7 mm
- net Net-(U6-+): track 0.00 -> 29.7 mm, vias 0 -> 1
- net Net-(D18-A): track 0.00 -> 26.7 mm
- net /A3 Supply/PDA_FB: track 0.00 -> 23.7 mm
- net /A2 Supply/-2KV: track 0.00 -> 22.6 mm
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- added copper zone on B.Cu, net +12V
- added copper zone on F.Cu, net /12V_IN
- added copper zone on F.Cu, net /A2 Supply/GATE_DRAIN
- added copper zone on F.Cu, net /A3 Supply/GATE_DRAIN
- added copper zone on F.Cu, net /Filament Supply/FILAMENT
- added copper zone on F.Cu, net /Filament Supply/MOS_DRAIN_FIL
- added copper zone on F.Cu, net /Filament Supply/MOS_SOURCE_FIL
- added copper zone on F.Cu, net AGND
- added copper zone on F.Cu, net AGND2
- added copper zone on B.Cu, net GND
- removed copper zone on F.Cu, net Net-(Q2-D)
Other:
- board size 108.6 x 131.8 mm -> 100 x 100 mm
- board text added: "+"
- board text added: "+12V GND"
- board text added: "+5V"
- board text added: "-"
- board text added: "400V 2KV"
- board text added: "400V-2KV x2 6.3V FILAMENT"
- board text added: "5.7V-6.4V"
- board text added: "A1"
- board text added: "A2"
- board text added: "A2 EN A2 OK"
- board text added: "A3"
- board text added: "A3 EN A3 OK"
- board text added: "AGND"
- board text added: "CRT High Voltage Supply V.4"
- board text added: "CRT Phosphor Types: Code: Flourescent color, Persistence time (phosphorescent color) P1: Green, Medium P2: Green, Medium-Long - P4: White, Medium-Short P5: Blue, Medium-Short - P7: Whitish-Blue, Long (Yellow) - P10: Reflective Pink, Long (non-emissive) P11: Actinic Blue, Medium-Short P12: Amber, Medium-Long - P15: Blue-Green, Very-short P16: Violet/UV-A, Very-short - P19: Amber, Long - P22: R,G,B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"
- board text added: "D3"
- board text added: "D4"
- board text added: "DISABLE HV BEFORE ADJUSTMENT"
- board text added: "DO NOT TOUCH OUTPUT"
- board text added: "ENABLE A2"
- board text added: "ENABLE A3"
- board text added: "ENABLE HEATER"
- board text added: "FIL ON"
- board text added: "G1"
- board text added: "H"
- board text added: "H+"
- board text added: "H-"
- board text added: "HEATER"
- board text added: "HV MAIN"
- board text added: "Just remember: ChatGPT said this project was too dangerous for me to make. I did it anyway."
- board text added: "K"
- board text added: "MEASURE A2 HERE (1:1000)"
- board text added: "MEASURE A3 HERE (1:1000)"
- board text added: "PLUG DDR5 INTO HV MAIN"
- board text added: "This board generates: H A2 A3 Deflection board generates: A1 from A2 D1 - D4 G1"
- board text added: "UP TO 4KV PRESENT"
- board text added: "chibitron.com"
- board text added: "do not aim beam at eyes"
- board text added: "viagra is not a soft-start but two diodes & an RC filter is."
- board text added: "why did you put an indicator LED here? This circuit literally powers a lightbulb."
- board text removed: "chibi"

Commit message: testload
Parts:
- added R86: 240, Resistor_SMD:R_0603_1608Metric, F.Cu at (115.8, 107.7)
- added R87: 3k, Resistor_SMD:R_0603_1608Metric, F.Cu at (117.6, 107.7)
- added R88: 3k, Resistor_SMD:R_0603_1608Metric, F.Cu at (115.0, 115.3)
- added R89: 240, Resistor_SMD:R_0603_1608Metric, F.Cu at (118.7, 111.3)
- C45: value C -> 4.7u
- R15: value R_US -> 12k
- R18, R50: value 30k -> 18.7k
- R20: value R_US -> 3k
- R21, R53: value 2.4k -> 2.49k
- R39, R7: value 10k -> 1k
- R72: value R_US -> 100k
- moved C35 9.56 mm to (117.0, 115.3), turned to -90 degrees
- moved C36 4.20 mm to (114.0, 107.7), turned to 90 degrees
- moved U6 4.10 mm to (116.0, 111.6), turned to -90 degrees
- moved TP4 3.20 mm to (120.1, 120.0)
- moved C33 1.70 mm to (124.1, 111.3)
- moved R49 1.70 mm to (122.3, 111.3)
- moved R52 1.70 mm to (120.5, 111.3)
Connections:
- C36 pad 1: Net-(U6-+) -> Net-(C36-Pad1)
- R52 pad 2: Net-(U6--) -> Net-(R52-Pad2)
- RV2 pad 2: Net-(U6-+) -> Net-(C36-Pad1)
- TP2 pad 1: Net-(U6-+) -> Net-(C36-Pad1)
- U6 pad 1: Net-(U6--) -> Net-(R52-Pad2)
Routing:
- net Net-(C36-Pad1): track 0.00 -> 28.7 mm, vias 0 -> 1
- net Net-(U6-+): track 29.7 -> 4.11 mm, vias 1 -> 0
- net +5V: track 160.0 -> 172.0 mm
- net Net-(R52-Pad2): track 0.00 -> 3.80 mm
- net AGND: track 11.6 -> 10.7 mm
- net Net-(U6--): track 5.68 -> 6.60 mm
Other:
- board text added: "CRT Phosphor Types: Code: Fluorescent color, Persistence time (phosphorescent color) P1: Green, Medium P2: Green, Medium-Long - P4: White, Medium-Short P5: Blue, Medium-Short - P7: Whitish-Blue, Long (Yellow) - P10: Reflective Pink, Long (non-emissive) P11: Actinic Blue, Medium-Short P12: Amber, Medium-Long - P15: Blue-Green, Very-short P16: Violet/UV-A, Very-short - P19: Amber, Long - P22: R,G,B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"
- board text removed: "CRT Phosphor Types: Code: Flourescent color, Persistence time (phosphorescent color) P1: Green, Medium P2: Green, Medium-Long - P4: White, Medium-Short P5: Blue, Medium-Short - P7: Whitish-Blue, Long (Yellow) - P10: Reflective Pink, Long (non-emissive) P11: Actinic Blue, Medium-Short P12: Amber, Medium-Long - P15: Blue-Green, Very-short P16: Violet/UV-A, Very-short - P19: Amber, Long - P22: R,G,B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"
